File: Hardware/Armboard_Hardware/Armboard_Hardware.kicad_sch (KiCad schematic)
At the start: 235 parts, among them J1 RJ45_LED_Shielded, Q41 BSS138, Q42 BSS138, Q43 T2N7002AK,LM, Q44 T2N7002AK,LM, Q45 T2N7002AK,LM, Q46 T2N7002AK,LM, Q47 T2N7002AK,LM, Q48 T2N7002AK,LM, Q49 T2N7002AK,LM, Q50 T2N7002AK,LM, Q51 T2N7002AK,LM, Q52 T2N7002AK,LM, Q63 AO3401A, SW1 SW_Push, SW10 SW_SPDT, SW11 SW_Push, SW12 SW_Push, SW2 SW_Push, SW3 SW_Push, SW4 SW_Push, SW5 SW_Push, SW6 SW_Push, SW7 SW_Push, SW8 SW_Push, SW9 SW_Push, U1 OKI, U10 VNH7070AS, U11 VNH7070AS, U12 VNH7070AS, U13 PCF8574, U14 VNH7070AS, U15 PCF8574, U16 PCF8574, U2 Teensy4.1_DEV-16771, U3 74LS148, U3 VNH7070AS, U36 OKI, U37 PCF8574, U38 PCF8574, U4 74LS148, U4 VNH7070AS, U5 74HC00, U5 VNH7070AS, U7 VNH7070AS, U8 VNH7070AS, U9 VNH7070AS

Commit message: Reworked Traces to match Arm Board size restraints
Reworked traces and power planes to meet size and power requirements for the VNH chip, and the size calculations for the new Arm Board Mount
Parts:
- C32, C34, C35, C36, C37, C38, C39, C40, C41: value 270uF -> 10uF
- C33: value 270uF -> 100uF
- Conn12, Conn13, Conn14, Conn15, Conn31, Conn32: footprint MRDT_Connectors:MOLEX_SL_04_Horizontal -> MRDT_Connectors:MOLEX_SL_04_Vertical
- Conn16, Conn27, Conn33: footprint MRDT_Connectors:MOLEX_SL_03_Horizontal -> MRDT_Connectors:MOLEX_SL_03_Vertical
- Conn17, Conn18, Conn19, Conn20, Conn21, Conn22, Conn23, Conn24, Conn25, Conn26, Conn29, Conn30: footprint MRDT_Connectors:MOLEX_SL_02_Horizontal -> MRDT_Connectors:MOLEX_SL_02_Vertical
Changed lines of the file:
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@@
   (junction (at 260.985 445.135) (diameter 0) (color 0 0 0 0)
   )
+  (junction (at 152.4 528.955) (diameter 0) (color 0 0 0 0)
+  )
   (junction (at 161.925 713.105) (diameter 0) (color 0 0 0 0)
   )
@@
     (stroke (width 0) (type default))
   )
-  (wire (pts (xy 152.4 516.89) (xy 152.4 516.255))
+  (wire (pts (xy 152.4 516.255) (xy 152.4 528.955))
     (stroke (width 0) (type default))
   )
@@
       (effects (font (size 1.524 1.524)) (justify left))
     )
-    (property "Footprint" "MRDT_Connectors:MOLEX_SL_04_Horizontal" (at 542.29 74.93 0)
+    (property "Footprint" "MRDT_Connectors:MOLEX_SL_04_Vertical" (at 542.29 74.93 0)
       (effects (font (size 1.524 1.524)) hide)
     )
@@
       (effects (font (size 1.27 1.27)))
     )
-    (property "Value" "270uF" (at 155.575 442.5221 90)
+    (property "Value" "10uF" (at 155.575 442.5221 90)
       (effects (font (size 1.27 1.27)))
     )
@@
       (effects (font (size 1.524 1.524)) (justify left))
     )
-    (property "Footprint" "MRDT_Connectors:MOLEX_SL_02_Horizontal" (at 800.1 94.615 0)
+    (property "Footprint" "MRDT_Connectors:MOLEX_SL_02_Vertical" (at 800.1 94.615 0)
       (effects (font (size 1.524 1.524)) hide)
     )
@@
       (effects (font (size 1.27 1.27)))
     )
-    (property "Value" "270uF" (at 156.845 360.6071 90)
+    (property "Value" "10uF" (at 156.845 360.6071 90)
       (effects (font (size 1.27 1.27)))
     )
@@
     )
   )
-  (symbol (lib_id "power:GND") (at 152.4 516.89 0) (unit 1)
-    (in_bom yes) (on_board yes) (dnp no) (fields_autoplaced)
-    (property "Reference" "#PWR027" (at 152.4 523.24 0)
-      (effects (font (size 1.27 1.27)) hide)
-    )
-    (property "Value" "GND" (at 152.4 521.0255 0)
-      (effects (font (size 1.27 1.27)))
-    )
-    (property "Footprint" "" (at 152.4 516.89 0)
-      (effects (font (size 1.27 1.27)) hide)
-    )
-    (property "Datasheet" "" (at 152.4 516.89 0)
-      (effects (font (size 1.27 1.27)) hide)
-    )
-    (pin "1")
-    (instances
-      (project "Armboard_Hardware"
-        (path "/4c7436f6-5ce4-4a98-b30c-5b440118f8cf"
-          (reference "#PWR027") (unit 1)
-        )
-      )
-    )
-  )
   (symbol (lib_id "power:GND") (at 521.335 173.99 0) (unit 1)
     (in_bom yes) (on_board yes) (dnp no) (fields_autoplaced)
@@
       (effects (font (size 1.524 1.524)) (justify left))
     )
-    (property "Footprint" "MRDT_Connectors:MOLEX_SL_03_Horizontal" (at 601.345 102.87 0)
+    (property "Footprint" "MRDT_Connectors:MOLEX_SL_03_Vertical" (at 601.345 102.87 0)
       (effects (font (size 1.524 1.524)) hide)
     )
@@
       (effects (font (size 1.524 1.524)) (justify left))
     )
-    (property "Footprint" "MRDT_Connectors:MOLEX_SL_02_Horizontal" (at 800.735 140.335 0)
+    (property "Footprint" "MRDT_Connectors:MOLEX_SL_02_Vertical" (at 800.735 140.335 0)
       (effects (font (size 1.524 1.524)) hide)
     )
@@
       (effects (font (size 1.524 1.524)) (justify left))
     )
-    (property "Footprint" "MRDT_Connectors:MOLEX_SL_03_Horizontal" (at 601.345 126.365 0)
+    (property "Footprint" "MRDT_Connectors:MOLEX_SL_03_Vertical" (at 601.345 126.365 0)
       (effects (font (size 1.524 1.524)) hide)
     )
@@
       (effects (font (size 1.27 1.27)))
     )
-    (property "Value" "270uF" (at 257.175 441.8871 90)
+    (property "Value" "10uF" (at 257.175 441.8871 90)
       (effects (font (size 1.27 1.27)))
     )
@@
       (effects (font (size 1.524 1.524)) (justify left))
     )
-    (property "Footprint" "MRDT_Connectors:MOLEX_SL_04_Horizontal" (at 541.655 138.43 0)
+    (property "Footprint" "MRDT_Connectors:MOLEX_SL_04_Vertical" (at 541.655 138.43 0)
       (effects (font (size 1.524 1.524)) hide)
     )
@@
       (effects (font (size 1.524 1.524)) (justify left))
     )
-    (property "Footprint" "MRDT_Connectors:MOLEX_SL_02_Horizontal" (at 759.46 94.615 0)
+    (property "Footprint" "MRDT_Connectors:MOLEX_SL_02_Vertical" (at 759.46 94.615 0)
       (effects (font (size 1.524 1.524)) hide)
     )
@@
       (effects (font (size 1.27 1.27)))
     )
-    (property "Value" "270uF" (at 258.445 360.6071 90)
+    (property "Value" "100uF" (at 258.445 360.6071 90)
       (effects (font (size 1.27 1.27)))
     )
@@
       (effects (font (size 1.524 1.524)) (justify left))
     )
-    (property "Footprint" "MRDT_Connectors:MOLEX_SL_02_Horizontal" (at 759.46 111.125 0)
+    (property "Footprint" "MRDT_Connectors:MOLEX_SL_02_Vertical" (at 759.46 111.125 0)
       (effects (font (size 1.524 1.524)) hide)
     )
@@
       (effects (font (size 1.524 1.524)) (justify left))
     )
-    (property "Footprint" "MRDT_Connectors:MOLEX_SL_02_Horizontal" (at 943.61 128.27 0)
+    (property "Footprint" "MRDT_Connectors:MOLEX_SL_02_Vertical" (at 943.61 128.27 0)
       (effects (font (size 1.524 1.524)) hide)
     )
@@
       (effects (font (size 1.524 1.524)) (justify left))
     )
-    (property "Footprint" "MRDT_Connectors:MOLEX_SL_02_Horizontal" (at 759.46 125.73 0)
+    (property "Footprint" "MRDT_Connectors:MOLEX_SL_02_Vertical" (at 759.46 125.73 0)
       (effects (font (size 1.524 1.524)) hide)
     )
@@
       (effects (font (size 1.27 1.27)))
     )
-    (property "Value" "270uF" (at 156.21 525.7071 90)
+    (property "Value" "10uF" (at 156.21 525.7071 90)
       (effects (font (size 1.27 1.27)))
     )
@@
       (effects (font (size 1.524 1.524)) (justify left))
     )
-    (property "Footprint" "MRDT_Connectors:MOLEX_SL_02_Horizontal" (at 800.1 111.125 0)
+    (property "Footprint" "MRDT_Connectors:MOLEX_SL_02_Vertical" (at 800.1 111.125 0)
       (effects (font (size 1.524 1.524)) hide)
     )
@@
       (effects (font (size 1.524 1.524)) (justify left))
     )
-    (property "Footprint" "MRDT_Connectors:MOLEX_SL_02_Horizontal" (at 760.095 154.94 0)
+    (property "Footprint" "MRDT_Connectors:MOLEX_SL_02_Vertical" (at 760.095 154.94 0)
       (effects (font (size 1.524 1.524)) hide)
     )
@@
       (effects (font (size 1.27 1.27)))
     )
-    (property "Value" "270uF" (at 158.75 608.2571 90)
+    (property "Value" "10uF" (at 158.75 608.2571 90)
       (effects (font (size 1.27 1.27)))
     )
@@
       (effects (font (size 1.524 1.524)) (justify left))
     )
-    (property "Footprint" "MRDT_Connectors:MOLEX_SL_02_Horizontal" (at 800.1 125.73 0)
+    (property "Footprint" "MRDT_Connectors:MOLEX_SL_02_Vertical" (at 800.1 125.73 0)
       (effects (font (size 1.524 1.524)) hide)
     )
@@
       (effects (font (size 1.524 1.524)) (justify left))
     )
-    (property "Footprint" "MRDT_Connectors:MOLEX_SL_03_Horizontal" (at 600.71 147.955 0)
+    (property "Footprint" "MRDT_Connectors:MOLEX_SL_03_Vertical" (at 600.71 147.955 0)
       (effects (font (size 1.524 1.524)) hide)
     )
@@
       (effects (font (size 1.27 1.27)))
     )
-    (property "Value" "270uF" (at 257.81 524.4371 90)
+    (property "Value" "10uF" (at 257.81 524.4371 90)
       (effects (font (size 1.27 1.27)))
     )
@@
       (effects (font (size 1.524 1.524)) (justify left))
     )
-    (property "Footprint" "MRDT_Connectors:MOLEX_SL_02_Horizontal" (at 800.735 154.94 0)
+    (property "Footprint" "MRDT_Connectors:MOLEX_SL_02_Vertical" (at 800.735 154.94 0)
       (effects (font (size 1.524 1.524)) hide)
     )
@@
       (effects (font (size 1.524 1.524)) (justify left))
     )
-    (property "Footprint" "MRDT_Connectors:MOLEX_SL_04_Horizontal" (at 541.655 177.8 0)
+    (property "Footprint" "MRDT_Connectors:MOLEX_SL_04_Vertical" (at 541.655 177.8 0)
       (effects (font (size 1.524 1.524)) hide)
     )
@@
       (effects (font (size 1.524 1.524)) (justify left))
     )
-    (property "Footprint" "MRDT_Connectors:MOLEX_SL_04_Horizontal" (at 541.655 158.75 0)
+    (property "Footprint" "MRDT_Connectors:MOLEX_SL_04_Vertical" (at 541.655 158.75 0)
       (effects (font (size 1.524 1.524)) hide)
     )
@@
       (effects (font (size 1.524 1.524)) (justify left))
     )
-    (property "Footprint" "MRDT_Connectors:MOLEX_SL_02_Horizontal" (at 760.095 140.335 0)
+    (property "Footprint" "MRDT_Connectors:MOLEX_SL_02_Vertical" (at 760.095 140.335 0)
       (effects (font (size 1.524 1.524)) hide)
     )
@@
       (effects (font (size 1.524 1.524)) (justify left))
     )
-    (property "Footprint" "MRDT_Connectors:MOLEX_SL_04_Horizontal" (at 542.29 115.57 0)
+    (property "Footprint" "MRDT_Connectors:MOLEX_SL_04_Vertical" (at 542.29 115.57 0)
       (effects (font (size 1.524 1.524)) hide)
     )
@@
       (effects (font (size 1.27 1.27)))
     )
-    (property "Value" "270uF" (at 260.35 608.2571 90)
+    (property "Value" "10uF" (at 260.35 608.2571 90)
       (effects (font (size 1.27 1.27)))
     )
@@
       (effects (font (size 1.27 1.27)))
     )
-    (property "Value" "270uF" (at 158.115 709.8571 90)
+    (property "Value" "10uF" (at 158.115 709.8571 90)
       (effects (font (size 1.27 1.27)))
     )
@@
       (effects (font (size 1.27 1.27)))
     )
-    (property "Value" "270uF" (at 259.715 709.2221 90)
+    (property "Value" "10uF" (at 259.715 709.2221 90)
       (effects (font (size 1.27 1.27)))
     )
@@
       (effects (font (size 1.524 1.524)) (justify left))
     )
-    (property "Footprint" "MRDT_Connectors:MOLEX_SL_02_Horizontal" (at 943.61 119.38 0)
+    (property "Footprint" "MRDT_Connectors:MOLEX_SL_02_Vertical" (at 943.61 119.38 0)
       (effects (font (size 1.524 1.524)) hide)
     )
@@
       (effects (font (size 1.524 1.524)) (justify left))
     )
-    (property "Footprint" "MRDT_Connectors:MOLEX_SL_04_Horizontal" (at 542.29 96.52 0)
+    (property "Footprint" "MRDT_Connectors:MOLEX_SL_04_Vertical" (at 542.29 96.52 0)
       (effects (font (size 1.524 1.524)) hide)
     )

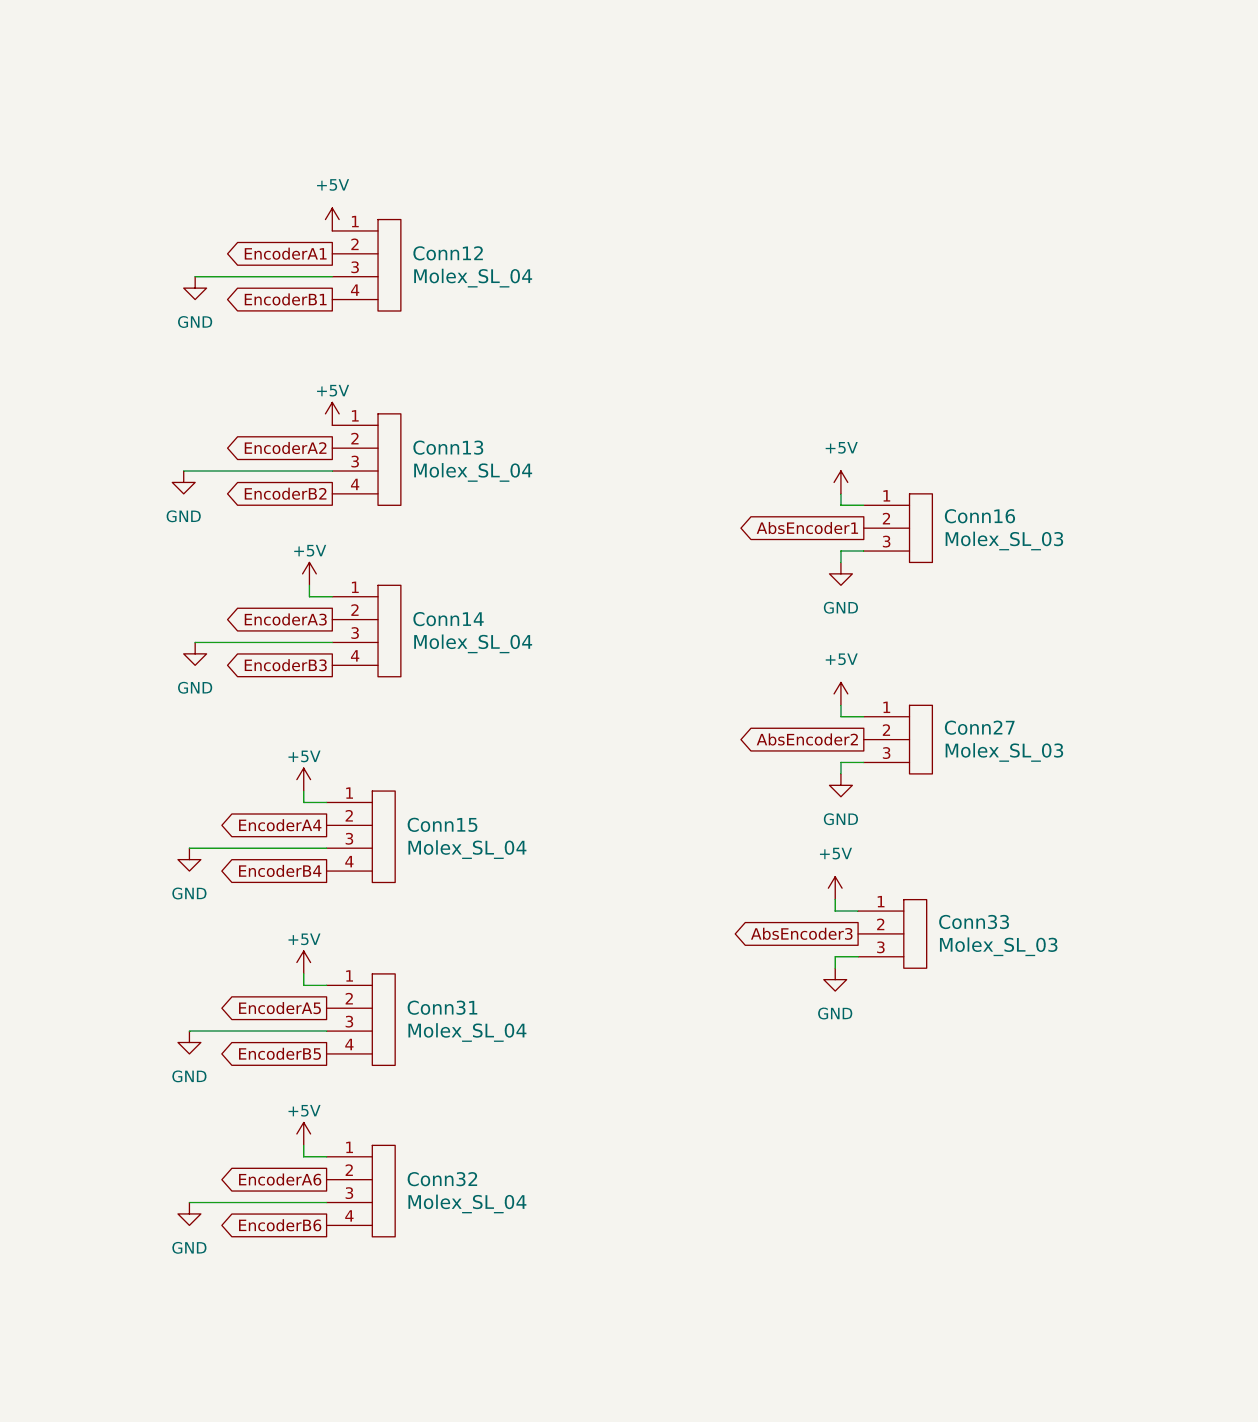
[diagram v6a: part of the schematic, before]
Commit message: Updated power planes, and routed traces
Updated power planes with proper priority levels and fixed the 12V plane to make it stretch through the VNH chips. Then routed traces for components
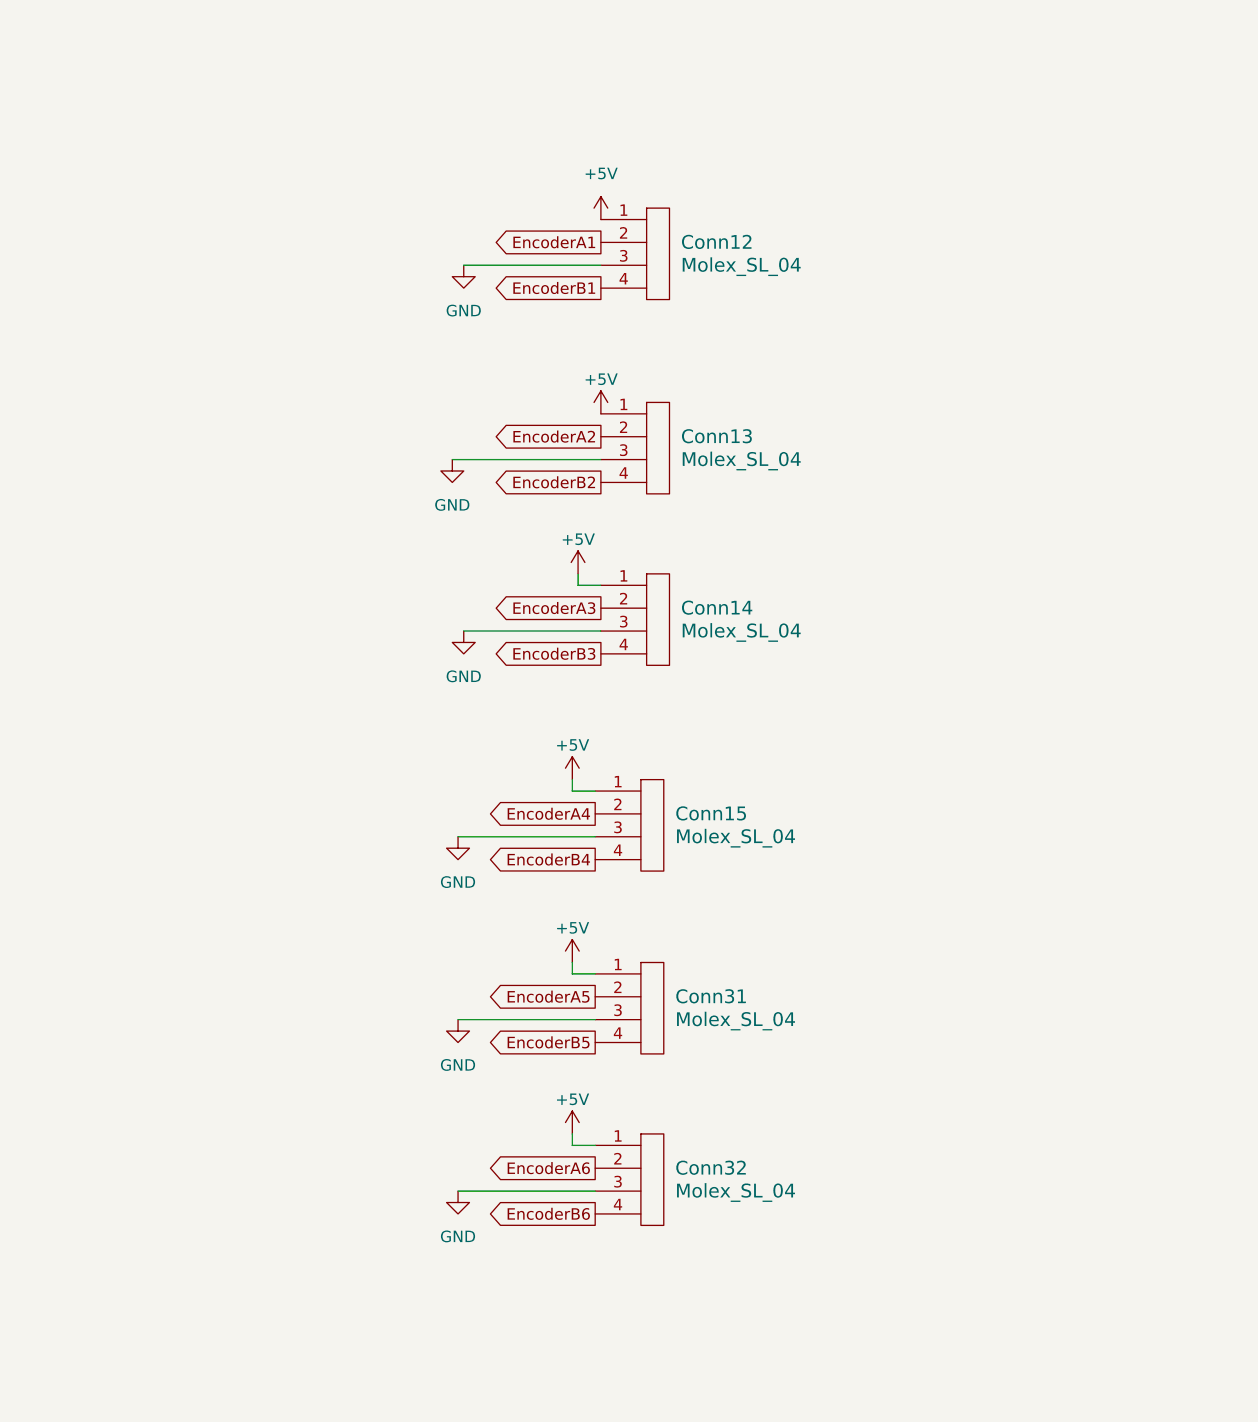
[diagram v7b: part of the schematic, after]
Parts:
- removed Conn16, Conn27, Conn33: Molex_SL_03, MRDT_Connectors:MOLEX_SL_03_Vertical, symbol MRDT_Connectors:Molex_SL_03
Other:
- moved on the sheet: Conn12, Conn13, Conn14, Conn15, Conn31, Conn32

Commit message: minor schematic changes and figured out (?) a layout for vnh circuit
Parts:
- removed C10, C12, C15, C16, C19, C20, C23, C31, C8: 10nF, Capacitor_SMD:C_0603_1608Metric_Pad1.08x0.95mm_HandSolder, symbol Device:C
- removed C30: 10 uF, Capacitor_SMD:C_0603_1608Metric_Pad1.08x0.95mm_HandSolder, symbol Device:C
- removed U16: PCF8574, Package_SO:SOIC-16W_7.5x10.3mm_P1.27mm, symbol Interface_Expansion:PCF8574
- added Conn11: Molex_SL_04, MRDT_Connectors:MOLEX_SL_04_Vertical, symbol MRDT_Connectors:Molex_SL_04
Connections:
- net AbsEncoder3 is gone; now on net DIR_SW: U2.5 (IN2)
- net +3V3: no longer Conn17.1, Conn18.1, Conn19.1, Conn20.1, Conn21.1, Conn22.1, Conn23.1, Conn24.1, Conn29.1, Conn30.1
- net +5V: now also Conn12.2, Conn13.2, Conn14.2, Conn15.2, Conn31.2, Conn32.2, Conn11.2; no longer Conn12.1, Conn13.1, Conn14.1, Conn15.1, Conn31.1, Conn32.1
- net EncoderA1: now also Conn12.3; no longer Conn12.2
- net EncoderA2: now also Conn13.3; no longer Conn13.2
- net EncoderA3: now also Conn14.3; no longer Conn14.2
- net EncoderA4: now also Conn15.3; no longer Conn15.2
- net EncoderA5: now also Conn31.3; no longer Conn31.2
- net EncoderA6: now also Conn32.3; no longer Conn32.2
- net GND: now also Conn12.1, Conn13.1, Conn14.1, Conn15.1, Conn17.2, Conn18.2, Conn19.2, Conn20.2, Conn21.2, Conn22.2, Conn23.2, Conn24.2, Conn29.2, Conn30.2, Conn31.1, Conn32.1, Conn11.1; no longer Conn12.3, Conn13.3, Conn14.3, Conn15.3, Conn31.3, Conn32.3
- net IN_A1: now also U38.9 (P4); no longer U38.10 (P5)
- net IN_A10: now also U15.11 (P6); no longer U15.12 (P7)
- net IN_A2: now also U38.11 (P6); no longer U38.12 (P7)
- net IN_A3: now also U13.4 (P0); no longer U13.5 (P1)
- net IN_A4: now also U13.6 (P2); no longer U13.7 (P3)
- net IN_A5: now also U13.9 (P4); no longer U13.10 (P5)
- net IN_A6: now also U13.11 (P6); no longer U13.12 (P7)
- net IN_A7: now also U15.4 (P0); no longer U15.5 (P1)
- net IN_A8: now also U15.6 (P2); no longer U15.7 (P3)
- net IN_A9: now also U15.9 (P4); no longer U15.10 (P5)
- net IN_B1: now also U38.10 (P5); no longer U38.11 (P6)
- net IN_B10: now also U15.12 (P7)
- net IN_B2: now also U38.12 (P7); no longer U13.4 (P0)
- net IN_B3: now also U13.5 (P1); no longer U13.6 (P2)
- net IN_B4: now also U13.7 (P3); no longer U13.9 (P4)
- net IN_B5: now also U13.10 (P5); no longer U13.11 (P6)
- net IN_B6: now also U13.12 (P7); no longer U15.4 (P0)
- net IN_B7: now also U15.5 (P1); no longer U15.6 (P2)
- net IN_B8: now also U15.7 (P3); no longer U15.9 (P4)
- net IN_B9: now also U15.10 (P5); no longer U15.11 (P6)
- net LIM_1: now also Conn17.1; no longer Conn17.2
- net LIM_10: now also Conn30.1; no longer Conn30.2
- net LIM_2: now also Conn18.1; no longer Conn18.2
- net LIM_3: now also Conn20.1; no longer Conn20.2
- net LIM_4: now also Conn23.1; no longer Conn23.2
- net LIM_5: now also Conn29.1; no longer Conn21.2
- net LIM_6: now also Conn21.1; no longer Conn19.2
- net LIM_7: now also Conn19.1; no longer Conn22.2
- net LIM_8: now also Conn22.1; no longer Conn24.2
- net LIM_9: now also Conn24.1; no longer Conn29.2
- net SEL10: now also U2.10 (CS1); no longer U38.9 (P4)
- net M5-: now reaches Conn6.1 (GND), U8.10 (OUT_B), U8.7 (OUT_B)
- net M1-: now reaches Conn2.1 (GND), U3.10 (OUT_B), U3.7 (OUT_B)
- net M1+: now reaches Conn2.2 (V+Log), U3.15 (OUT_A), U3.2 (OUT_A)
- net M10-: now reaches Conn34.1 (GND), U14.10 (OUT_B), U14.7 (OUT_B)
- net M6-: now reaches Conn8.1 (GND), U10.10 (OUT_B), U10.7 (OUT_B)
- net M9-: now reaches Conn10.1 (GND), U12.10 (OUT_B), U12.7 (OUT_B)
- net M9+: now reaches Conn10.2 (V+Log), U12.15 (OUT_A), U12.2 (OUT_A)
- net M5+: now reaches Conn6.2 (V+Log), U8.15 (OUT_A), U8.2 (OUT_A)
- net M4-: now reaches Conn5.1 (GND), U7.10 (OUT_B), U7.7 (OUT_B)
- net M4+: now reaches Conn5.2 (V+Log), U7.15 (OUT_A), U7.2 (OUT_A)
- net M2-: now reaches Conn3.1 (GND), U4.10 (OUT_B), U4.7 (OUT_B)
- net M3+: now reaches Conn4.2 (V+Log), U5.15 (OUT_A), U5.2 (OUT_A)
- net M8-: now reaches Conn9.1 (GND), U11.10 (OUT_B), U11.7 (OUT_B)
- net M8+: now reaches Conn9.2 (V+Log), U11.15 (OUT_A), U11.2 (OUT_A)
- net M10+: now reaches Conn34.2 (V+Log), U14.15 (OUT_A), U14.2 (OUT_A)
- net M6+: now reaches Conn8.2 (V+Log), U10.15 (OUT_A), U10.2 (OUT_A)
- net M3-: now reaches Conn4.1 (GND), U5.10 (OUT_B), U5.7 (OUT_B)
- net M2+: now reaches Conn3.2 (V+Log), U4.15 (OUT_A), U4.2 (OUT_A)
- net M7-: now reaches Conn7.1 (GND), U9.10 (OUT_B), U9.7 (OUT_B)
- net M7+: now reaches Conn7.2 (V+Log), U9.15 (OUT_A), U9.2 (OUT_A)
- net AbsEncoder1 renamed EncoderB7
- net EncoderB7: now also Conn11.4
- net AbsEncoder2 renamed EncoderA7
- net EncoderA7: now also Conn11.3
- net CS1 renamed CS
- no-connect marks 25 -> 17
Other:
- moved on the sheet: Conn10A, Conn10B, Conn12, Conn13, Conn14, Conn15, Conn2A, Conn2B, Conn31, Conn32, Conn34A, Conn34B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
